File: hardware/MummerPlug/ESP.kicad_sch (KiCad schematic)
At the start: 8 parts

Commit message: assign footprint to esp symbol
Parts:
- U?: footprint (none) -> mummerplug:ESP8684-MINI-1
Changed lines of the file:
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@@
     (property "Reference" "U?" (id 0) (at 158.75 58.1912 0))
     (property "Value" "ESP8684-MINI" (id 1) (at 158.75 60.7312 0))
-    (property "Footprint" "" (id 2) (at 121.285 92.71 0)
+    (property "Footprint" "mummerplug:ESP8684-MINI-1" (id 2) (at 121.285 92.71 0)
       (effects (font (size 1.27 1.27)) hide)
     )

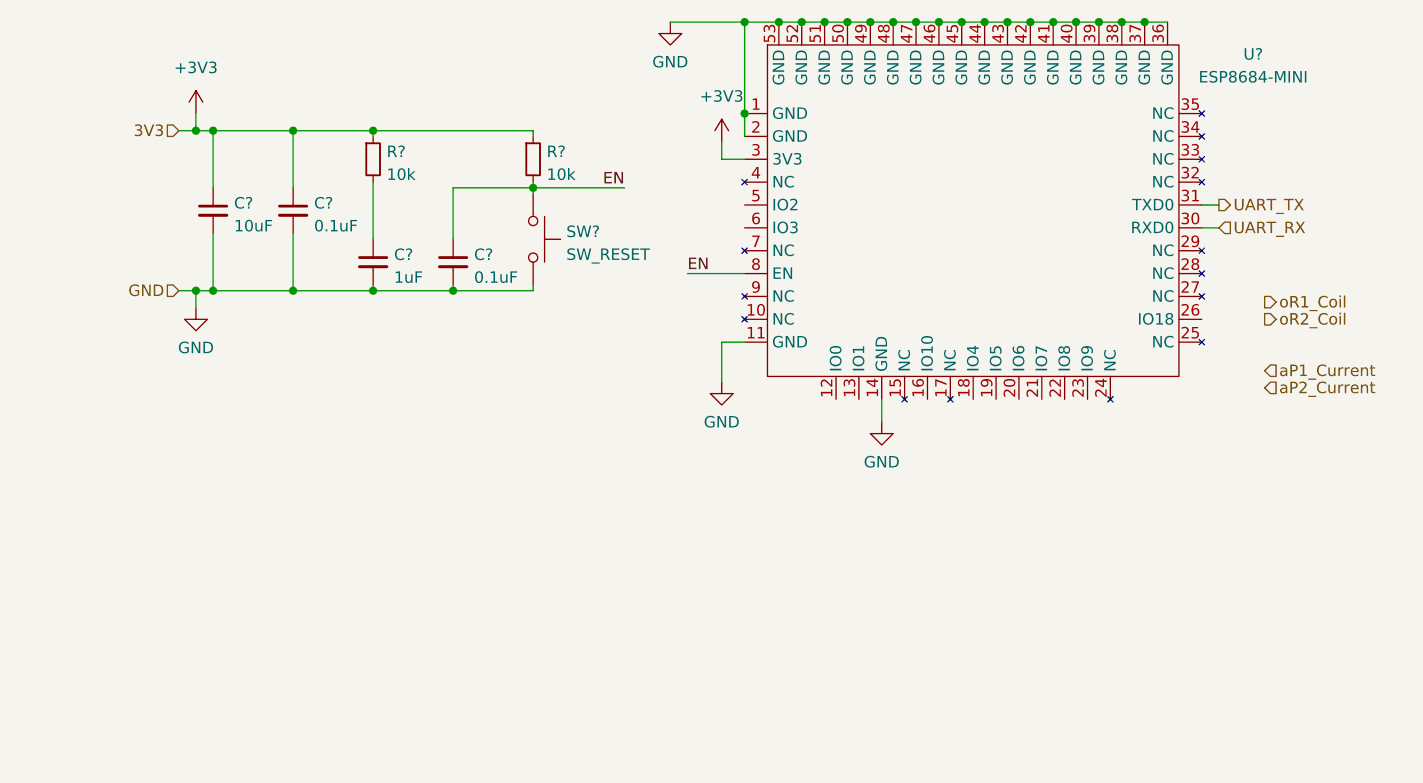
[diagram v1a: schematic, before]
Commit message: fix enable pin
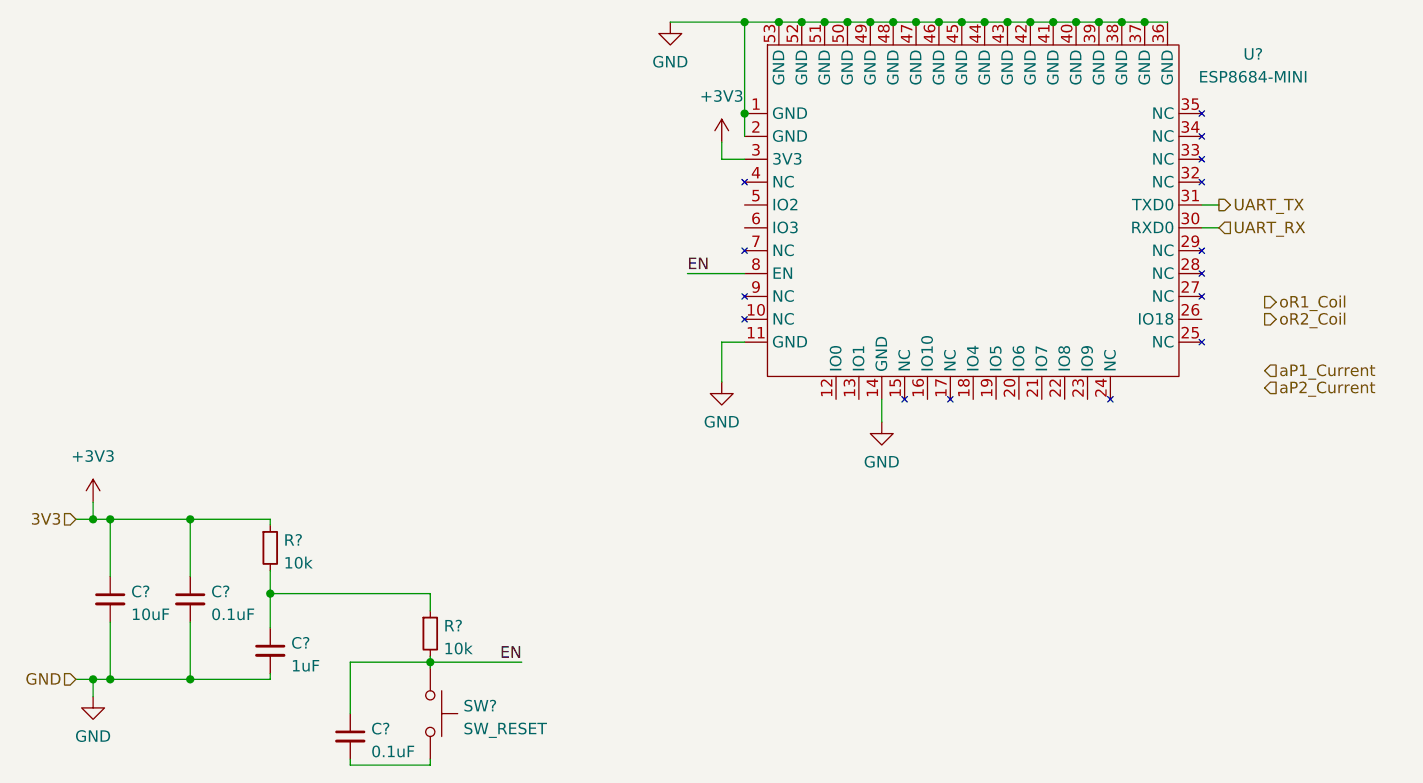
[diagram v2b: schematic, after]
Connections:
- net +3V3: no longer R?.1
- net GND: no longer C?.2, SW?.2
- net at C?.1, R?.2: now also R?.1
- new net: C?.2, SW?.2
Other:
- moved on the sheet: C?, R?, SW?
